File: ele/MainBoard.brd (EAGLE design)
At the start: 134.9 x 100 mm, 116 parts, among them IC1 MCP23017SP, IC2 74HC595D, IC3 74HC595D, X1 POWER_IN, X2 POWER_OUT

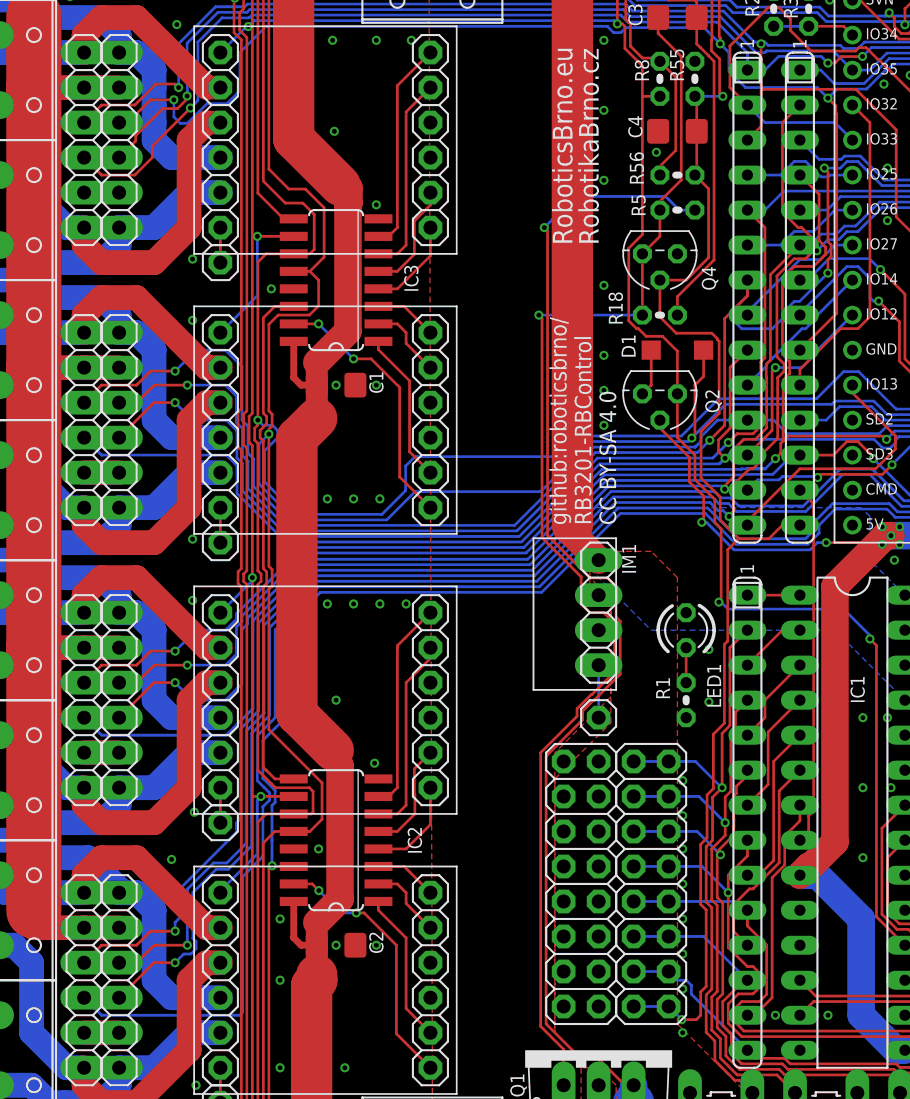
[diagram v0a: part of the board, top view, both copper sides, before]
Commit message: ele: MainBoard - fix position, names, labels of motors pinheads and terminals block
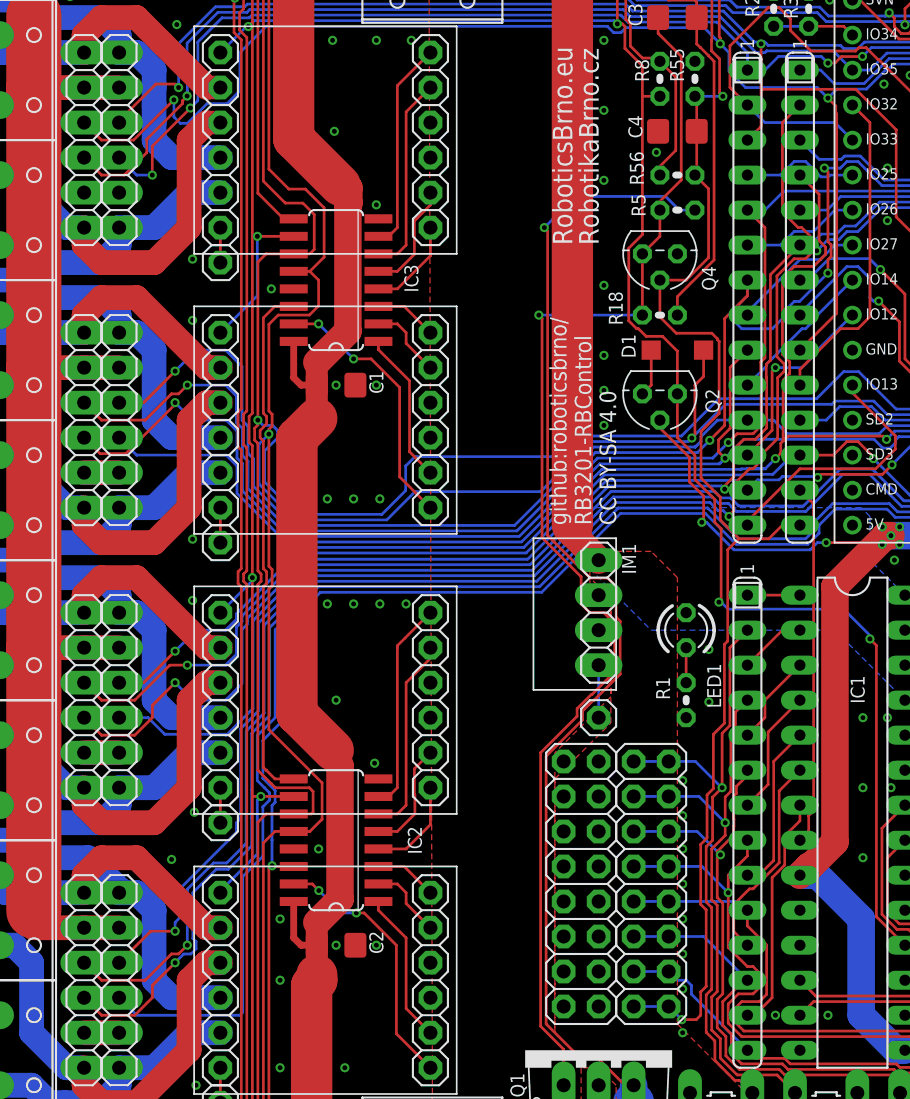
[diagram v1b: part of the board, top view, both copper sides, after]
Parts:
- JP31: value ENC1 -> M2
- JP32: value ENC3 -> M4
- JP33: value ENC5 -> M6
- JP34: value ENC7 -> M8
- JP35: value ENC2 -> M1
- JP36: value ENC4 -> M3
- JP37: value ENC6 -> M5
- JP38: value ENC8 -> M7
- X10: value (none) -> M7
- X3: value (none) -> M2
- X4: value (none) -> M4
- X5: value (none) -> M6
- X6: value (none) -> M8
- X7: value (none) -> M1
- X8: value (none) -> M3
- X9: value (none) -> M5
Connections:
- net ENC1A: now also JP35.3; no longer JP31.3
- net ENC1B: now also JP35.4; no longer JP31.4
- net ENC2A: now also JP31.3; no longer JP35.3
- net ENC2B: now also JP31.4; no longer JP35.4
- net ENC3A: now also JP36.3; no longer JP32.3
- net ENC3B: now also JP36.4; no longer JP32.4
- net ENC4A: now also JP32.3; no longer JP36.3
- net ENC4B: now also JP32.4; no longer JP36.4
- net ENC5A: now also JP37.3; no longer JP33.3
- net ENC5B: now also JP37.4; no longer JP33.4
- net ENC6A: now also JP33.3; no longer JP37.3
- net ENC6B: now also JP33.4; no longer JP37.4
- net ENC7A: now also JP38.3; no longer JP34.3
- net ENC7B: now also JP38.4; no longer JP34.4
- net ENC8A: now also JP34.3; no longer JP38.3
- net ENC8B: now also JP34.4; no longer JP38.4
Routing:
- net ENC8B: track 107.2 -> 111.3 mm
- net ENC4B: track 119.6 -> 123.7 mm
- net ENC2B: track 164.7 -> 168.8 mm
- net ENC8A: track 137.0 -> 140.5 mm
- net ENC6A: track 136.0 -> 139.6 mm
- net ENC4A: track 117.3 -> 120.9 mm
- net ENC2A: track 138.4 -> 142.0 mm
- net ENC6B: track 132.9 -> 136.4 mm
- net ENC5B: track 151.0 -> 148.5 mm
- net ENC3B: track 130.3 -> 127.7 mm
- net ENC1A: track 151.1 -> 148.6 mm
- net ENC5A: track 143.2 -> 140.6 mm
- net ENC1B: track 160.6 -> 158.1 mm
- net ENC7A: track 160.8 -> 158.3 mm
- net ENC3A: track 132.3 -> 129.9 mm
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
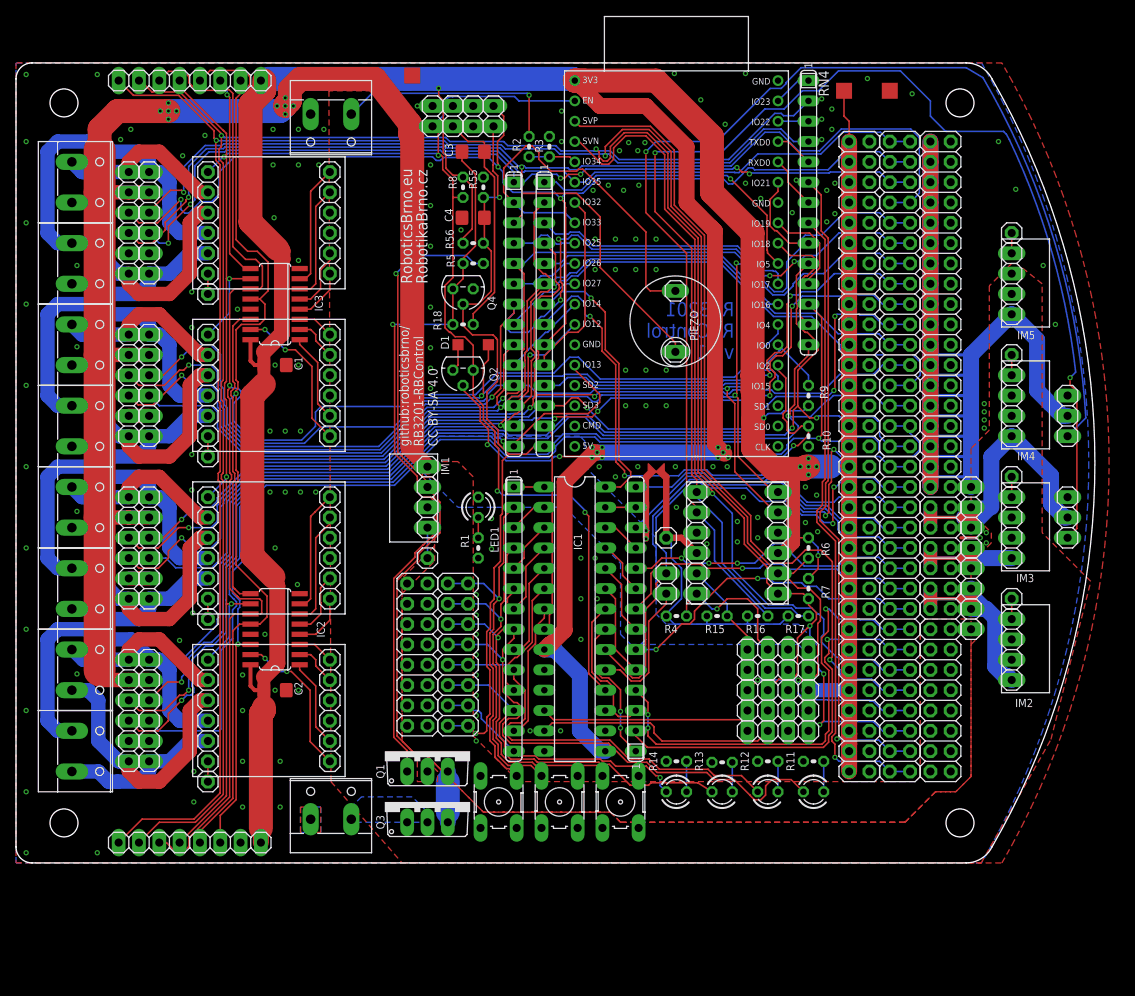
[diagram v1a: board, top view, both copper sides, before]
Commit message: ele: MainBoard - add diode to ESP32 +5V, add jumper for PIEZO ON/OFF
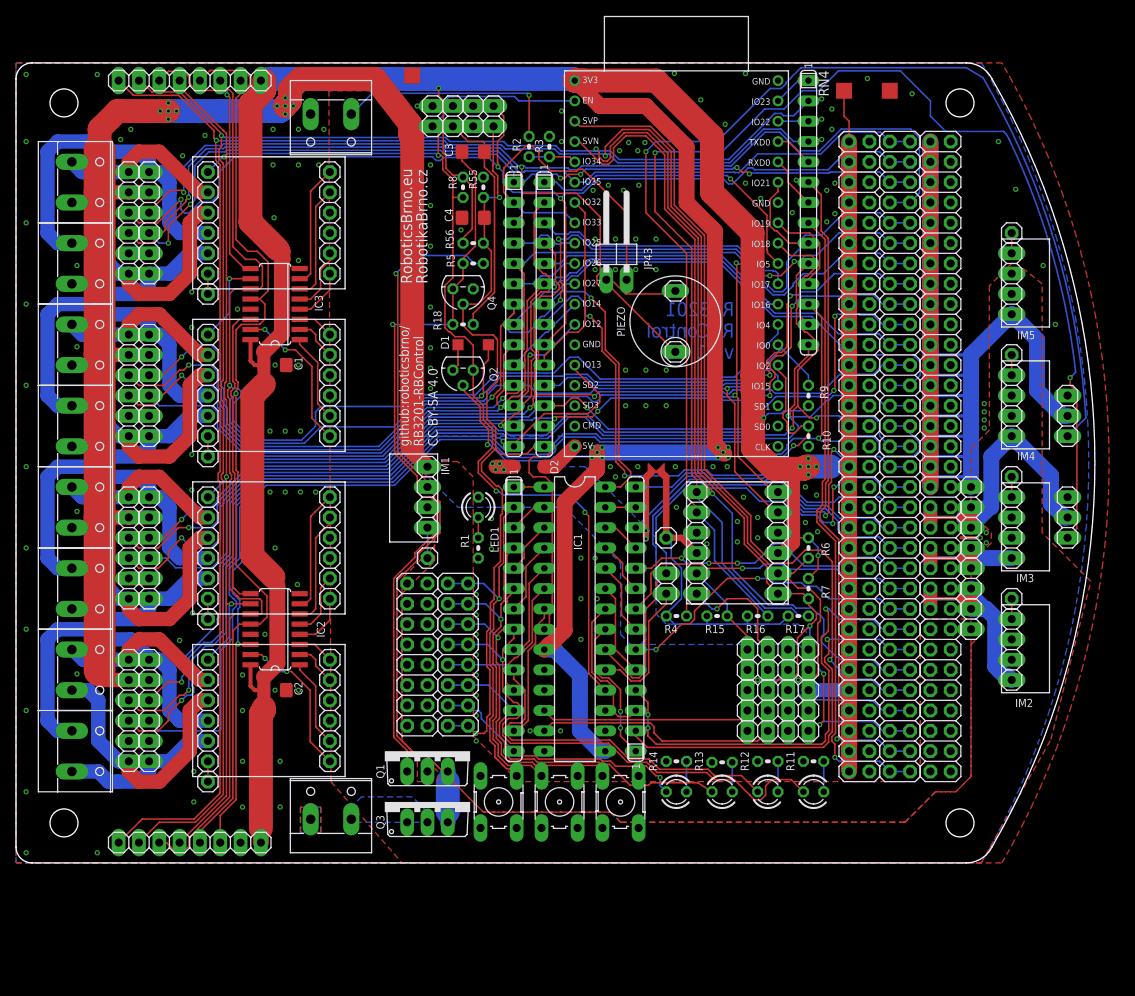
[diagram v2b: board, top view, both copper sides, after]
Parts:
- added D2: (no value), diode:SOD123
- added JP43: PIEZO_ON, pinhead:1X02/90
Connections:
- new net +5V_ESP: D2.C, IM6.19
- new net N$3: JP43.1, PIEZO.-
- net +5V: now also D2.A; no longer IM6.19
- net ENC7B_: now also JP43.2; no longer PIEZO.-
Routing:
- net N$3: track 0.00 -> 9.53 mm
- net ENC7B_: track 48.3 -> 42.5 mm
- net +5V_ESP: track 0.00 -> 4.87 mm
- net ESP_!SHUTDOWN!_: track 26.2 -> 30.5 mm
- net ESP_!SHUTDOWN: track 100.3 -> 103.2 mm
- net +5V: track 202.4 -> 205.1 mm, vias 12 -> 16
- net +3V3: track 531.1 -> 533.1 mm, vias 20 -> 19
- net EN: track 264.9 -> 266.3 mm
- net ENC7A: track 158.3 -> 159.4 mm
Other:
- board text added: "PIEZO ON"

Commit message: ele: MainBoard - repair problem with pin IO12, change nets around piezo, change some names and labels
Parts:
- removed LED5: BLUE/WHITE, led:LED3MM
- added LEDP: (no value), led:LED3MM
- added R19, R20: 10k, rcl_upravena:0204V
- JP21: value ? -> RESET
- LED1: value (none) -> RED
- LED2: value RED -> YELLOW
- LED3: value YELLOW -> GREEN
- LED4: value GREEN -> BLUE/WHITE
- moved LED1 55.0 mm to (99.7, 8.89), turned to 0 degrees
- moved LED3 5.72 mm to (88.3, 8.89)
- moved LED4 5.72 mm to (82.5, 8.89)
- moved LED2 5.71 mm to (94.0, 8.89)
- renumbered S1 to SW1, S2 to SW2, S3 to SW3
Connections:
- net N$3 renamed PIEZO
- removed net N$10: LED2.K, R11.1
- removed net N$15: LED3.K, R12.1
- removed net N$16: LED4.K, R13.1
- removed net N$17: LED5.K, R14.1
- new net LED1: LED1.K, R11.1
- new net LED2: LED2.K, R12.1
- new net LED3: LED3.K, R13.1
- new net LED4: LED4.K, R14.1
- net +3V3: now also R20.1
- net +5V: now also LEDP.A; no longer LED1.A
- net EB3: now also LED1.A; no longer LED2.A
- net EB4: now also LED2.A; no longer LED3.A
- net EB5: now also LED3.A; no longer LED4.A
- net EB6: now also LED4.A; no longer LED5.A
- net ENC5A: now also RN5.12; no longer RN5.11
- net ENC5A_: now also IM6.26, RN5.11; no longer IM6.13, RN5.12
- net ENC7A: now also JP43.2; no longer PIEZO.+
- net ENC7B_: now also PIEZO.+; no longer JP43.2
- net GND: now also R19.1
- net N$9: now also LEDP.K; no longer LED1.K
- net SCKMOT: now also IM6.13, R19.2, R20.2; no longer IM6.26
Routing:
- net ENC5A_: track 14.4 -> 0.00 mm, vias 1 -> 0
- net ENC7A: track 159.4 -> 148.3 mm
- net ENC7B_: track 42.5 -> 34.1 mm
- net ENC5A: track 140.6 -> 136.5 mm
- net N$17: track 3.81 -> 0.00 mm
- net N$15: track 3.81 -> 0.00 mm
- net N$10: track 3.81 -> 0.00 mm
- net LED4: track 0.00 -> 3.81 mm
- net LED2: track 0.00 -> 3.81 mm
- net LED1: track 0.00 -> 3.81 mm
- net N$16: track 3.68 -> 0.00 mm
- net LED3: track 0.00 -> 3.68 mm
- net SCKMOT: track 209.8 -> 208.6 mm
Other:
- board text added: "OFF"
- board text added: "ON"
- board text added: "SW1"
- board text added: "SW2"
- board text added: "SW3"
- board text removed: "B0"
- board text removed: "B1"
- board text removed: "B2"
- board text removed: "B3"
- board text removed: "B4"
- board text removed: "B5"
- board text removed: "B6"
- board text removed: "START BTN"
- board text removed: "STOP BTN"

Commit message: ele: Previous changes routed into the PCB.
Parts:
- R2: value (none) -> 82k
- R3: value (none) -> 10k
- moved R19 30.5 mm to (18.9, 90.9)
- moved R20 22.7 mm to (12.8, 7.37), turned to 180 degrees
- moved PIEZO 10.5 mm to (81.2, 62.6), turned to 0 degrees
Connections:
- net ENC7A: now also JP43.1; no longer JP43.2
- net PIEZO: now also JP43.2; no longer JP43.1
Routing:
- net ENC5A_: track 0.00 -> 40.7 mm, vias 0 -> 1
- net +3V3: track 533.1 -> 552.5 mm
- net ENC7B_: track 34.1 -> 49.4 mm
- net SCKMOT: track 208.6 -> 198.9 mm
- net ENC5A: track 136.5 -> 143.6 mm, vias 4 -> 5
- net RCKMOT: track 211.5 -> 216.7 mm
- net ENC7A: track 148.3 -> 145.7 mm
- net PIEZO: track 9.53 -> 11.5 mm
- net ENC4B: track 123.7 -> 124.5 mm
